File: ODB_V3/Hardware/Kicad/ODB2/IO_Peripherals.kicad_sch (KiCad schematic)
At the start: 22 parts, among them IC1 W25Q512JVEIQ, J2 IdeFIX_Conn_01x04, J3 SYS_SW_Conn_01x05_Header, J5 MEM2067, J6 RFD_Conn_01x05_Header

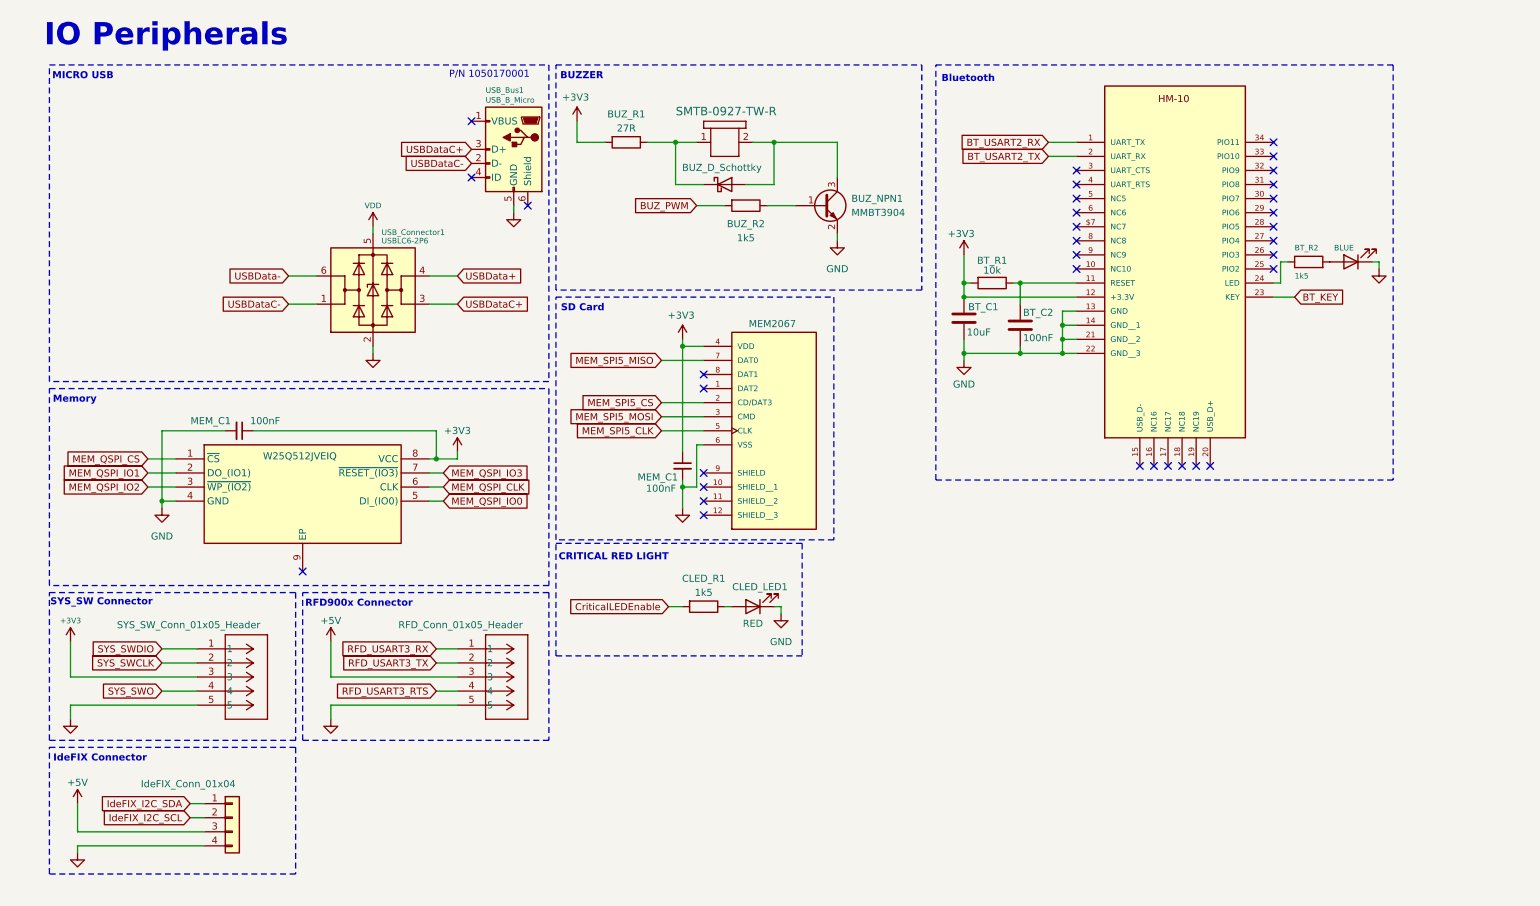
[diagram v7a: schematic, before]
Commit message: fix: switch ferrite bead filtre, add gps connector to main
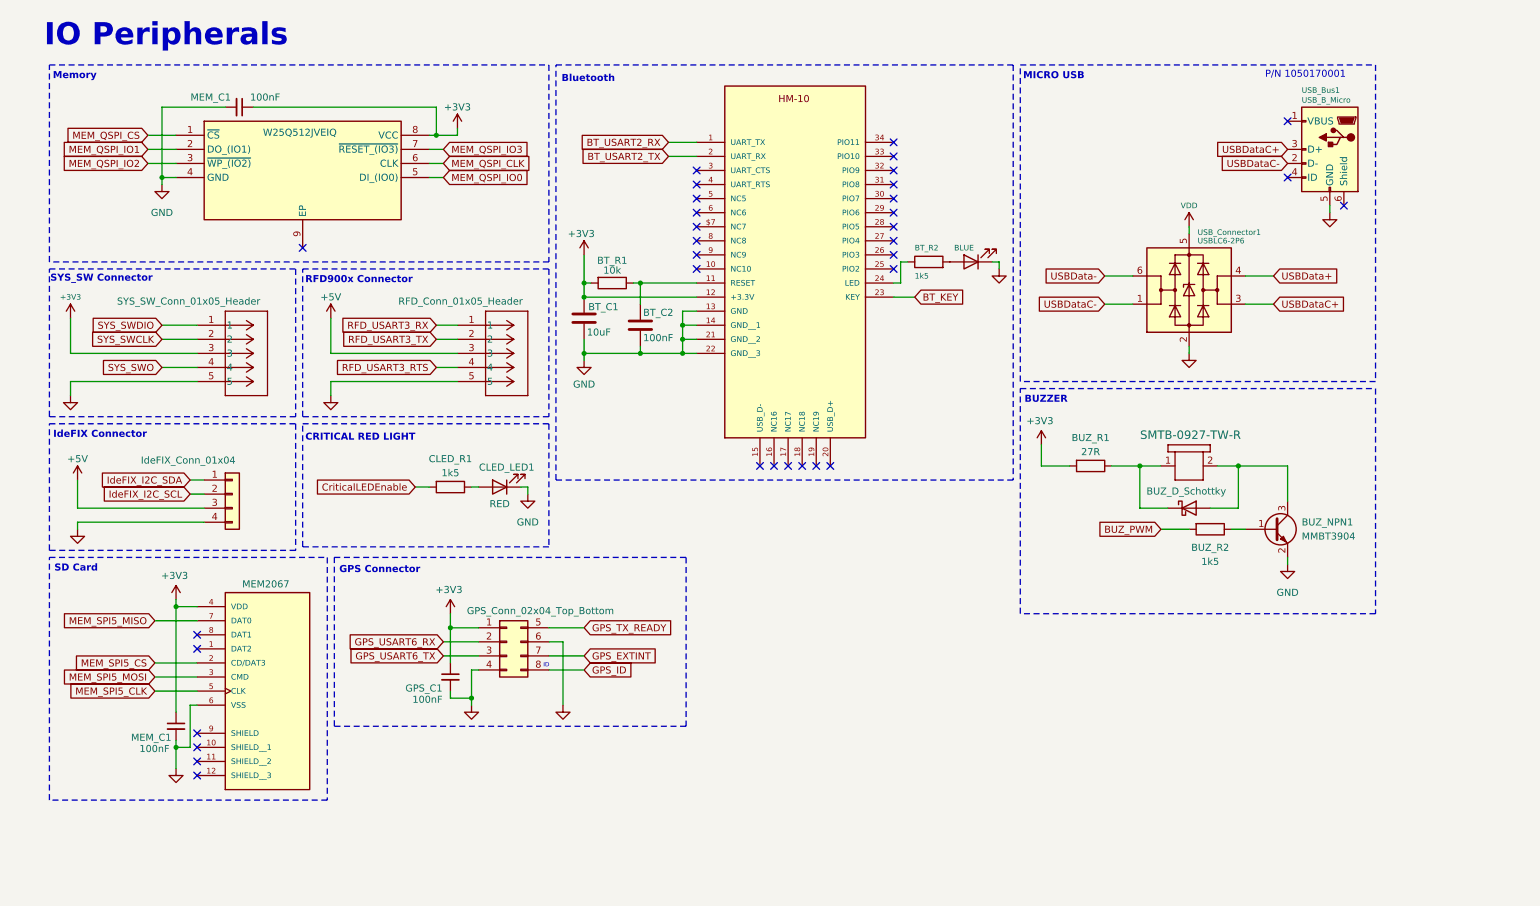
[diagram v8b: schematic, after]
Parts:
- added GPS_C1: 100nF, Capacitor_SMD:C_0603_1608Metric, symbol Device:C_Small
- added J1: GPS_Conn_02x04_Top_Bottom, Connector_PinHeader_2.00mm:PinHeader_2x04_P2.00mm_Horizontal, symbol Connector_Generic:Conn_02x04_Top_Bottom
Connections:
- net +3V3: now also GPS_C1.1, J1.1 (Pin_1)
- net GND: now also GPS_C1.2, J1.4 (Pin_4), J1.6 (Pin_6)
- new net GPS_EXTINT: J1.7 (Pin_7)
- new net GPS_ID: J1.8 (Pin_8)
- new net GPS_TX_READY: J1.5 (Pin_5)
- new net GPS_USART6_RX: J1.2 (Pin_2)
- new net GPS_USART6_TX: J1.3 (Pin_3)
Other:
- note added: "GPS Connector"
- note added: "ID"
- moved on the sheet: BT_C1, BT_C2, BT_R1, BT_R2, BUZ_NPN1, BUZ_R1, BUZ_R2, CLED_LED1, CLED_R1, MEM_C1, USB_Bus1, USB_Connector1
